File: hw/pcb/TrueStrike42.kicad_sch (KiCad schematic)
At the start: 187 parts, among them U1 ProMicro, U10 4053, U2 74HC4051, U3 74HC4051, U4 74HC4051, U5 74HC4051, U6 74HC4051, U7 74HC4051, U8 74HC4051, U9 74AHCT125

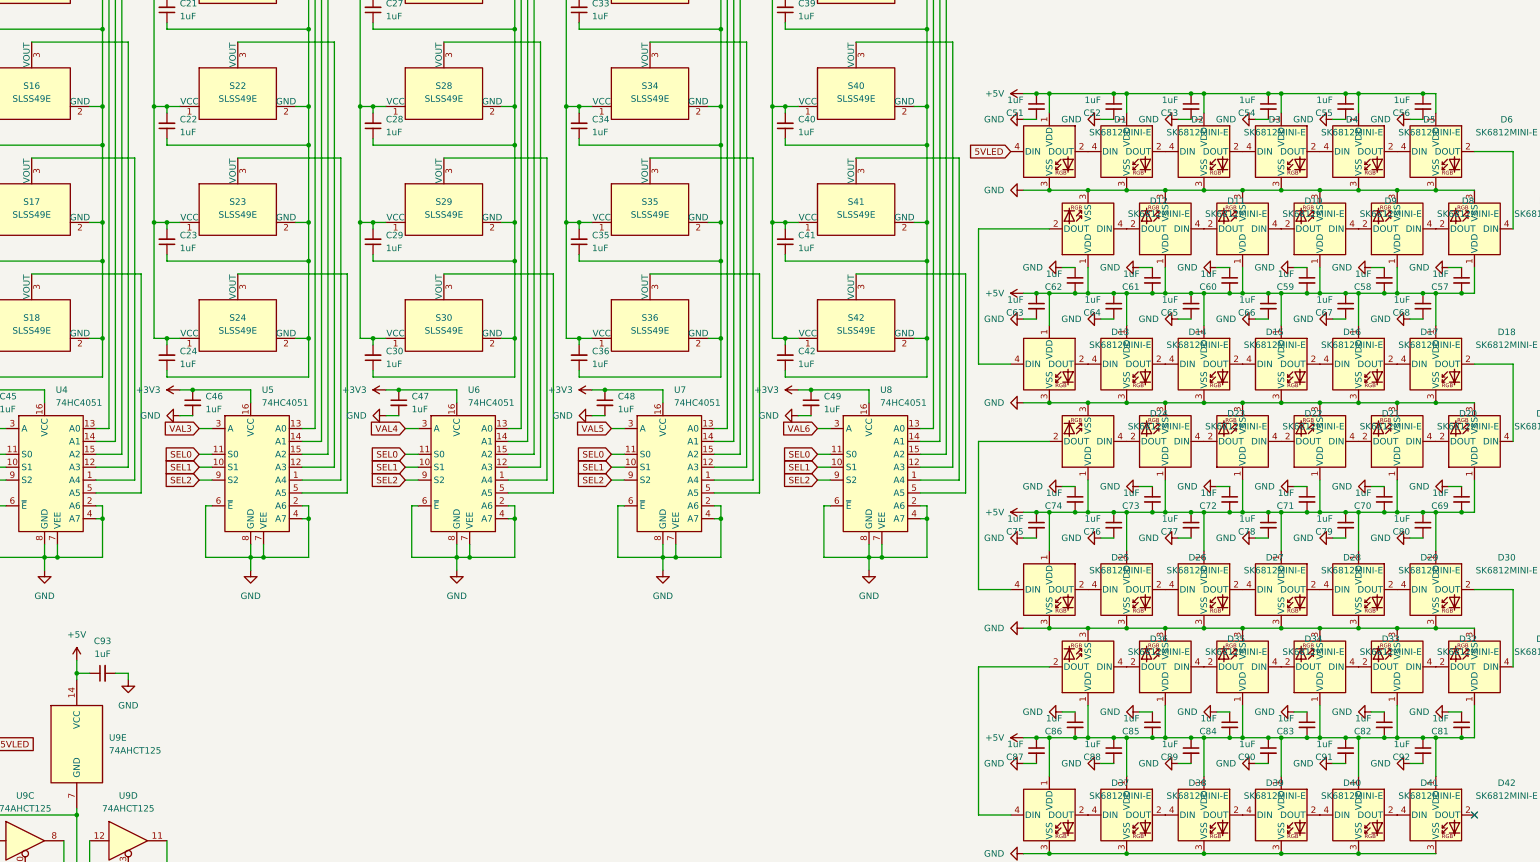
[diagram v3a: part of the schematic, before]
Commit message: Update TrueStrike42.kicad_sch
Remove unnecessary capacitors
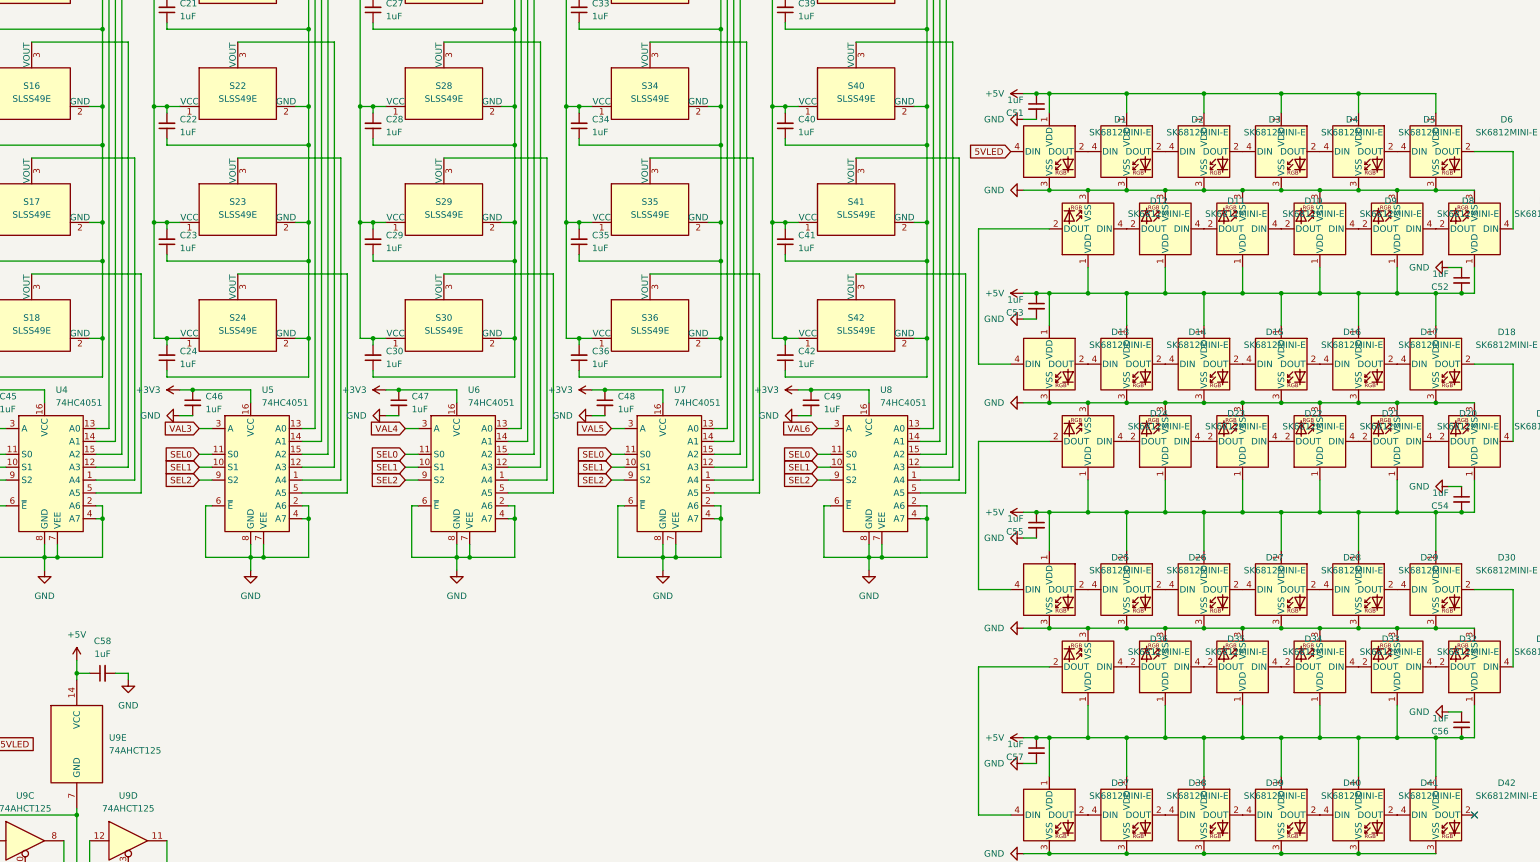
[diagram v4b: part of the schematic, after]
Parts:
- removed C52, C53, C54, C55, C56, C58, C59, C60, C61, C62, C64, C65, C66, C67, C68, C70, C71, C72, C73, C74, C76, C77, C78, C79, C80, C82, C83, C84, C85, C86, C88, C89, C90, C91, C92: 1uF, Capacitor_SMD:C_0805_2012Metric_Pad1.18x1.45mm_HandSolder, symbol Device:C_Small
- renumbered C57 to C52, C63 to C53, C69 to C54, C75 to C55, C81 to C56, C87 to C57, C93 to C58

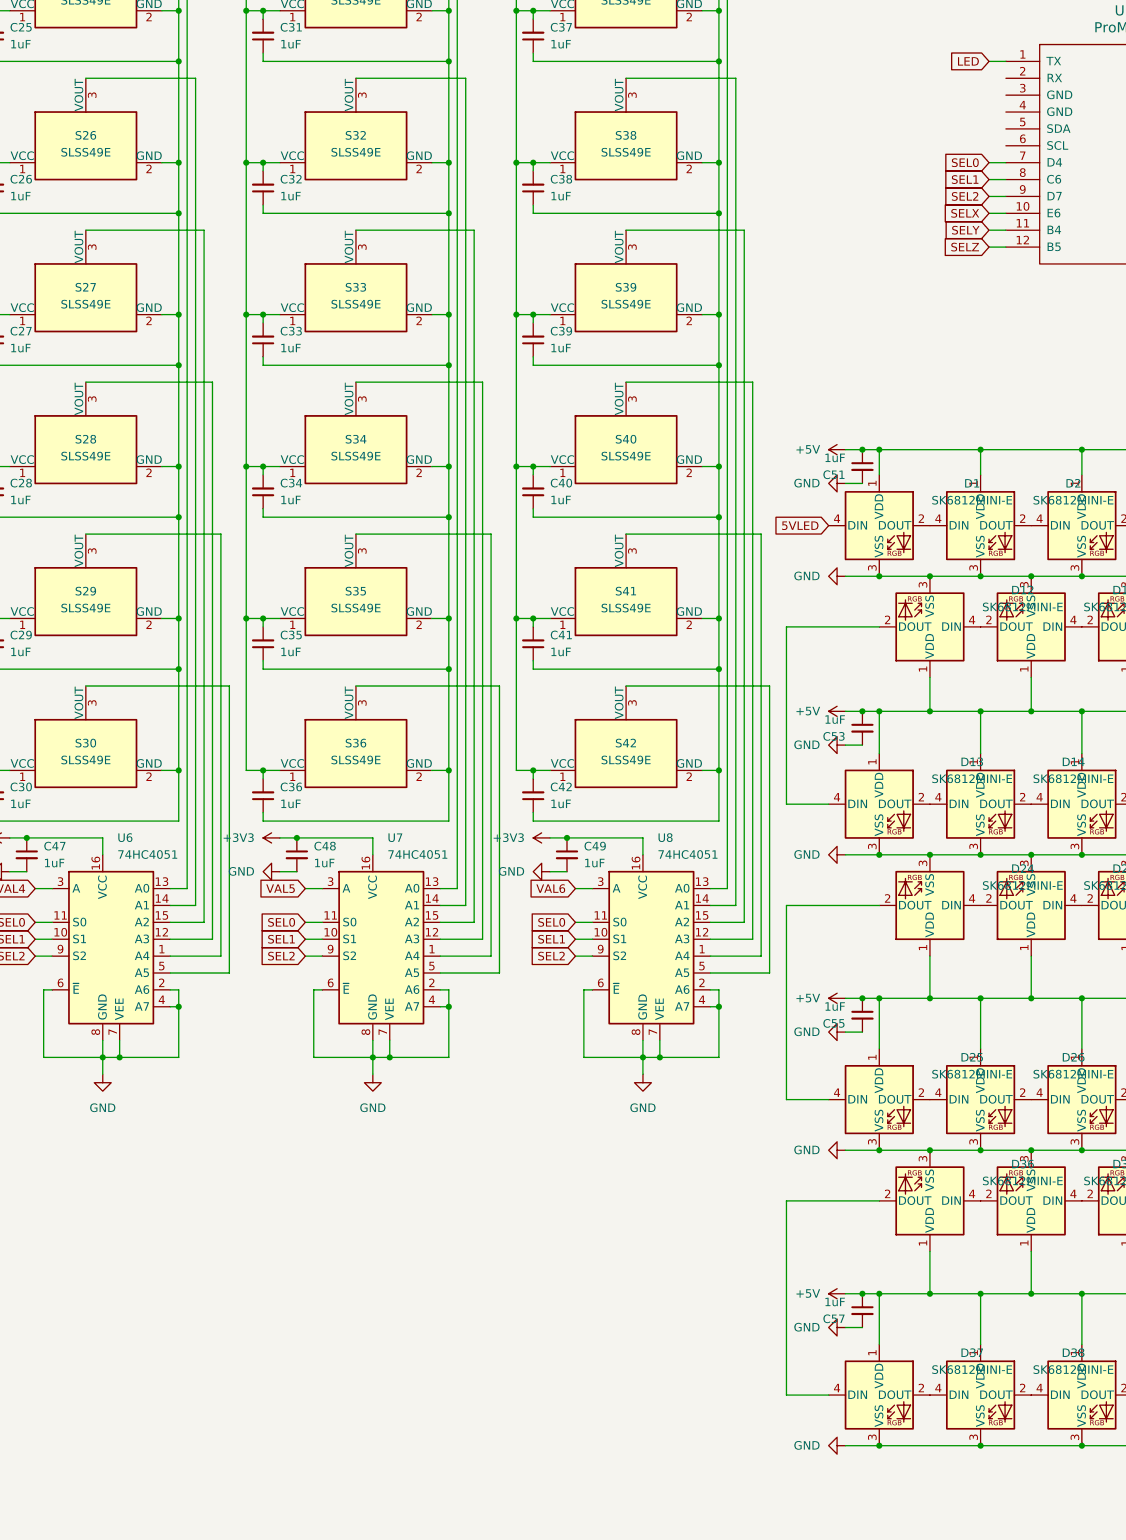
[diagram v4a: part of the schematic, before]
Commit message: Add LED screen and a reset switch
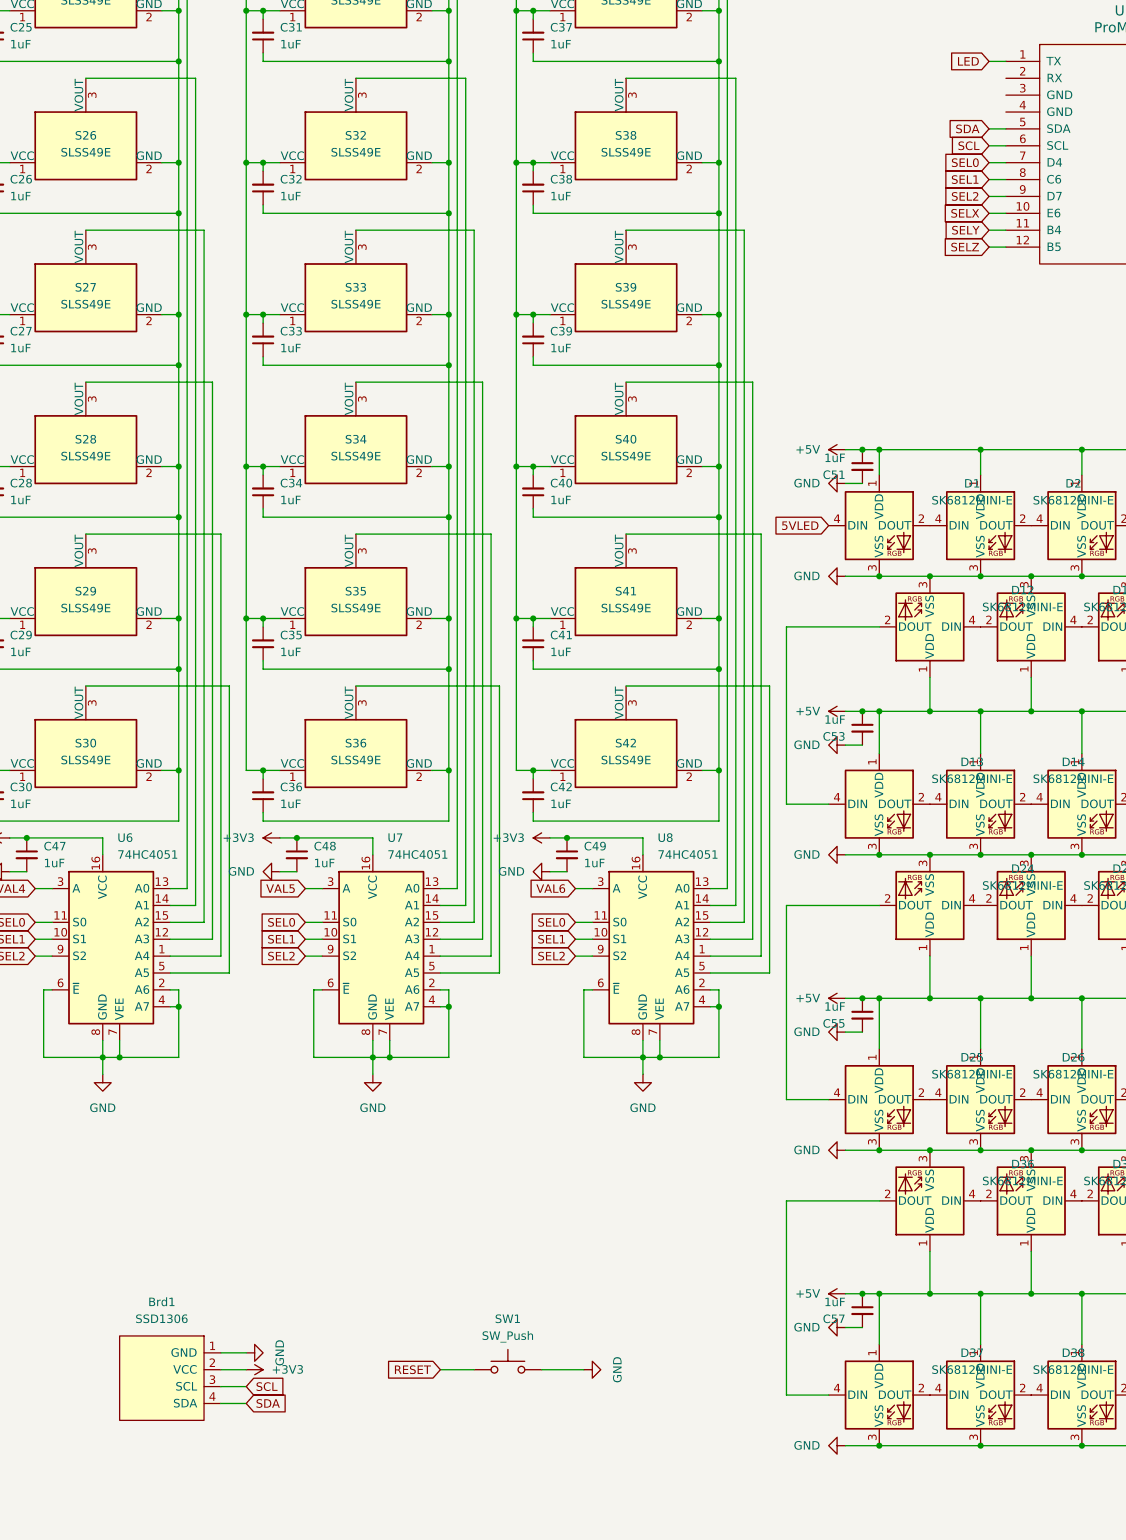
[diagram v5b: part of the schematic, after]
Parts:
- added Brd1: SSD1306, SSD1306:128x64OLED, symbol SSD1306-128x64:SSD1306
- added SW1: SW_Push, Button_Switch_SMD:SW_Tactile_SPST_NO_Straight_CK_PTS636Sx25SMTRLFS, symbol Switch:SW_Push
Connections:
- net +3V3: now also Brd1.2 (VCC)
- net GND: now also Brd1.1 (GND), SW1.2
- net RESET: now also SW1.1
- net SDA: now reaches U1.5 (SDA)
- net SDA: now also Brd1.4 (SDA)
- net SCL: now reaches U1.6 (SCL)
- net SCL: now also Brd1.3 (SCL)

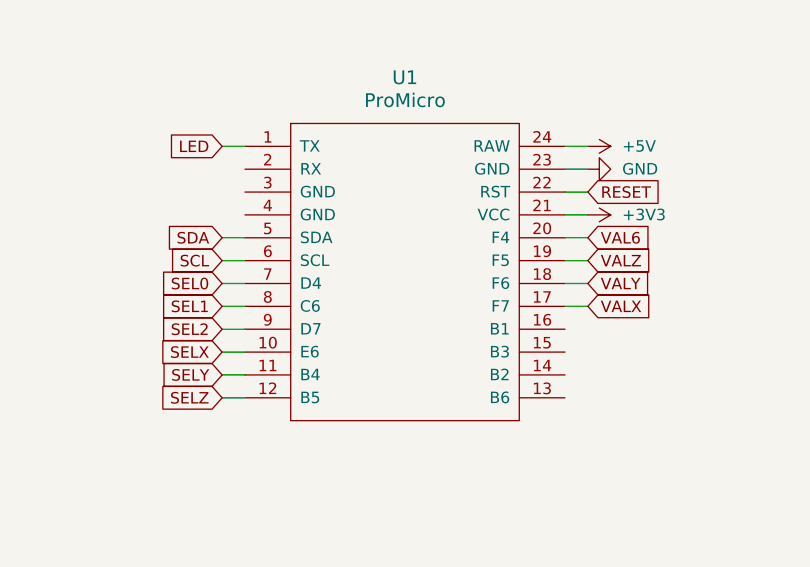
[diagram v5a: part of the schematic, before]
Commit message: Update functional silkscreens
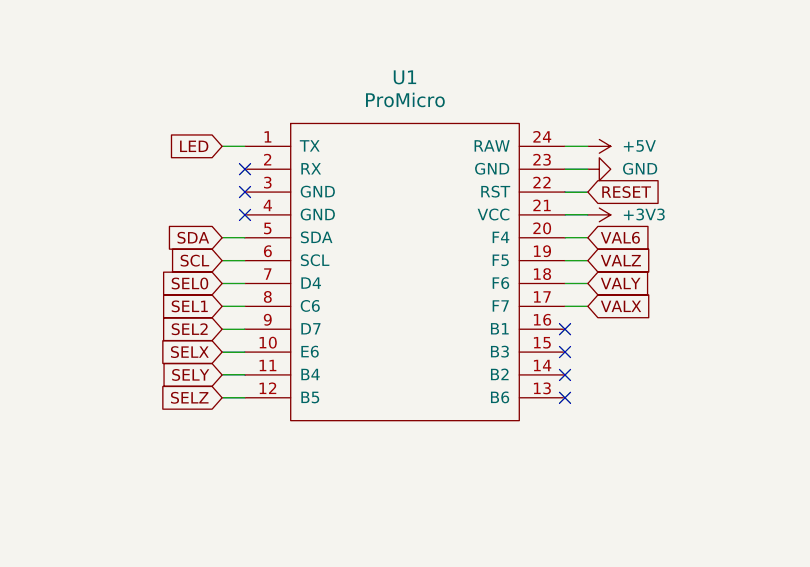
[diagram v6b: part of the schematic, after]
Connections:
- no-connect marks 1 -> 8
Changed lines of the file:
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@@
+	)
+	(no_connect
+		(at 368.3 68.58)
+	)
+	(no_connect
+		(at 332.74 48.26)
+	)
+	(no_connect
+		(at 332.74 45.72)
+	)
+	(no_connect
+		(at 368.3 60.96)
+	)
+	(no_connect
+		(at 332.74 43.18)
 	)
 	(no_connect
 		(at 397.51 241.3)
 	)
+	(no_connect
+		(at 368.3 63.5)
+	)
+	(no_connect
+		(at 368.3 66.04)
+	)
 	(wire
